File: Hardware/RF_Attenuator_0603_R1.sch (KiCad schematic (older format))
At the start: 5 parts, among them J3 SMA_Wurth_60312242114510

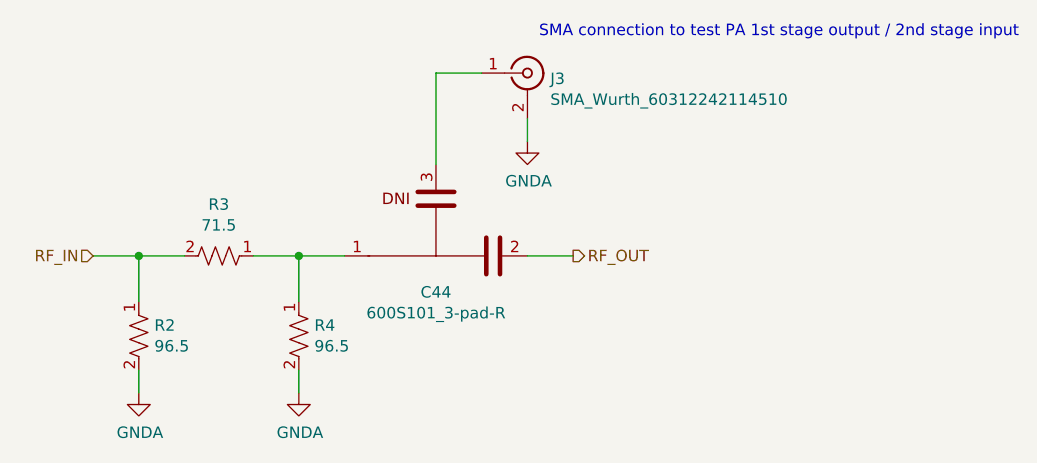
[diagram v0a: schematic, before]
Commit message: Major cleanup to both the schematic and directory structure. Stackup has changed accomodate to 0.65mm trace width. Chebyshev filter lived through the experience in the Qucs simulation; others not checked yet. I do want to re-visit the matching networks of all of the amplifiers as I have developed some good strategies to implement them.
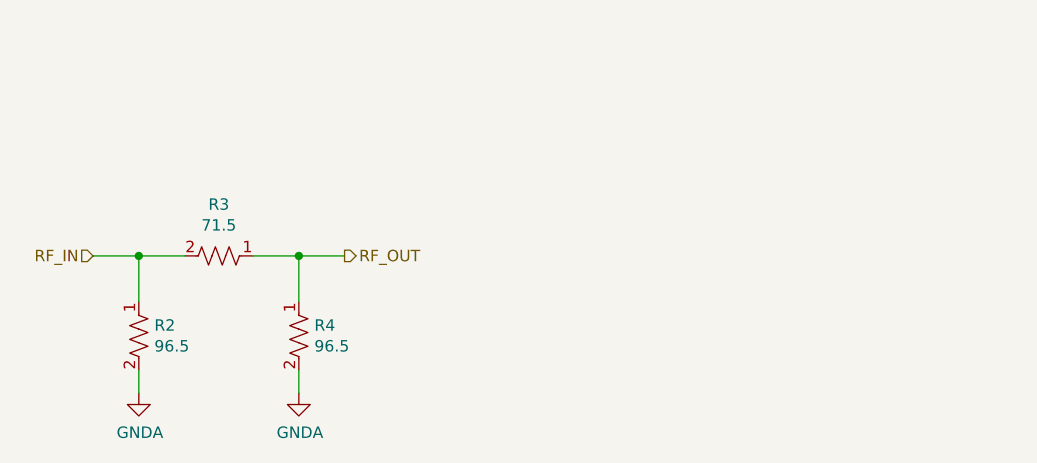
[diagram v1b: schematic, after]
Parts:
- removed C44: 600S101_3-pad-R, Capacitor_SMD:C_0603_1608Metric_3-pad-R, symbol ATC:600S101_3-pad-R
- removed J3: SMA_Wurth_60312242114510, RF:SMA_Wurth_60312242114510, symbol RF:SMA_Wurth_60312242114510
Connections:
- net RF_OUT: now also R3.1, R4.1
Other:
- note removed: "SMA connection to test PA 1st stage output / 2nd stage input"
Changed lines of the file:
@@
 $Descr A4 11693 8268
 encoding utf-8
-Sheet 15 16
+Sheet 17 22
 Title ""
 Date ""
@@
 	4650 3650 4850 3650
 Connection ~ 4850 3650
-Text Notes 8700 2700 2    50   ~ 0
-SMA connection to test PA 1st stage output / 2nd stage input
-Text HLabel 6750 3650 2    50   Output ~ 0
+Text HLabel 5750 3650 2    50   Output ~ 0
 RF_OUT
 Wire Wire Line
-	5550 3650 5750 3650
+	5750 3650 5550 3650
 Connection ~ 5550 3650
-Wire Wire Line
-	6550 3050 6550 3150
-$Comp
-L power:GNDA #PWR?
-U 1 1 5F2B6F4E
-P 6550 3150
-AR Path="/5F1FE880/5F2B6F4E" Ref="#PWR?"  Part="1"
-AR Path="/5F19C733/5F2B6F4E" Ref="#PWR?"  Part="1"
-AR Path="/5F19DDB3/5F2B6F4E" Ref="#PWR?"  Part="1"
-AR Path="/5F11BFA6/5F2B6F4E" Ref="#PWR?"  Part="1"
-AR Path="/5F11C68E/5F2B6F4E" Ref="#PWR?"  Part="1"
-AR Path="/5F20A94F/5F2B6F4E" Ref="#PWR?"  Part="1"
-AR Path="/5F20D989/5F2B6F4E" Ref="#PWR?"  Part="1"
-AR Path="/5F20DB0B/5F2B6F4E" Ref="#PWR?"  Part="1"
-AR Path="/5F2751D2/5F2B6F4E" Ref="#PWR?"  Part="1"
-AR Path="/5F19BA77/5F2B6F4E" Ref="#PWR052"  Part="1"
-F 0 "#PWR052" H 6550 2900 50  0001 C CNN
-F 1 "GNDA" H 6555 2977 50  0000 C CNN
-F 2 "" H 6550 3150 50  0001 C CNN
-F 3 "" H 6550 3150 50  0001 C CNN
-	1    6550 3150
-	1    0    0    -1
-$EndComp
-Wire Wire Line
-	6150 2850 6350 2850
-$Comp
-L RF:SMA_Wurth_60312242114510 J?
-U 1 1 5F2B6F3F
-P 6550 2850
-AR Path="/5F20DB0B/5F2B6F3F" Ref="J?"  Part="1"
-AR Path="/5F20A94F/5F2B6F3F" Ref="J?"  Part="1"
-AR Path="/5F2751D2/5F2B6F3F" Ref="J?"  Part="1"
-AR Path="/5F19BA77/5F2B6F3F" Ref="J3"  Part="1"
-F 0 "J3" H 6650 2825 50  0000 L CNN
-F 1 "SMA_Wurth_60312242114510" H 6650 2734 50  0000 L CNN
-F 2 "RF:SMA_Wurth_60312242114510" H 6550 2850 50  0001 C CNN
-F 3 "https://www.we-online.de/katalog/datasheet/60312242114510.pdf" H 6550 2850 50  0001 C CNN
-	1    6550 2850
-	1    0    0    -1
-$EndComp
-Wire Wire Line
-	6750 3650 6550 3650
-$Comp
-L ATC:600S101_3-pad-R C44
-U 1 1 5F3AA005
-P 6150 3650
-F 0 "C44" H 6150 3809 50  0000 C CNN
-F 1 "600S101_3-pad-R" H 6150 3900 50  0000 C CNN
-F 2 "Capacitor_SMD:C_0603_1608Metric_3-pad-R" H 7050 2900 50  0001 C CNN
-F 3 "" V 6150 3600 50  0001 C CNN
-	1    6150 3650
-	-1   0    0    1
-$EndComp
-Wire Wire Line
-	6150 2850 6150 3250
 $EndSCHEMATC
